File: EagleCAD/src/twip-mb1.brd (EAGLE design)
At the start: 81 x 88.9 mm, 11 parts, among them U1 GY-521MPU6050

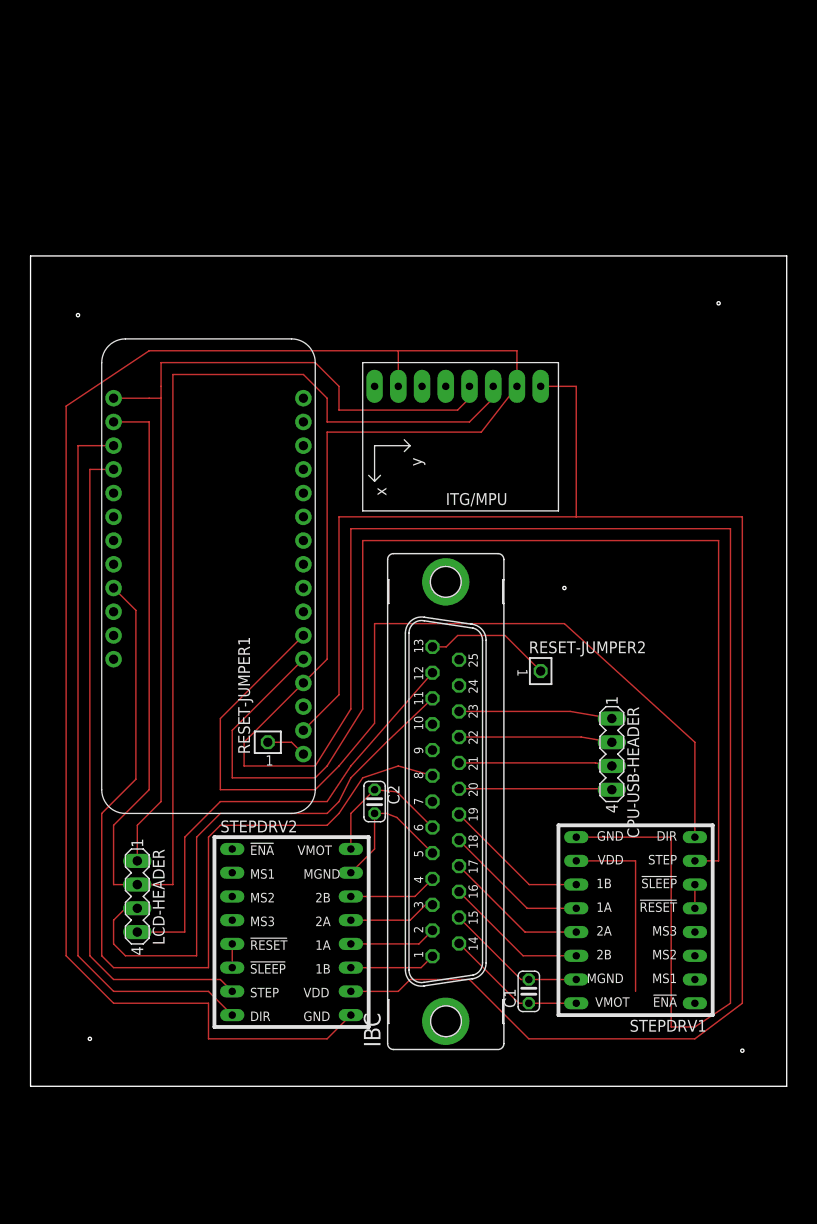
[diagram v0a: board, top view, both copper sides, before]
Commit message: fix LCD header, as decoupling caps
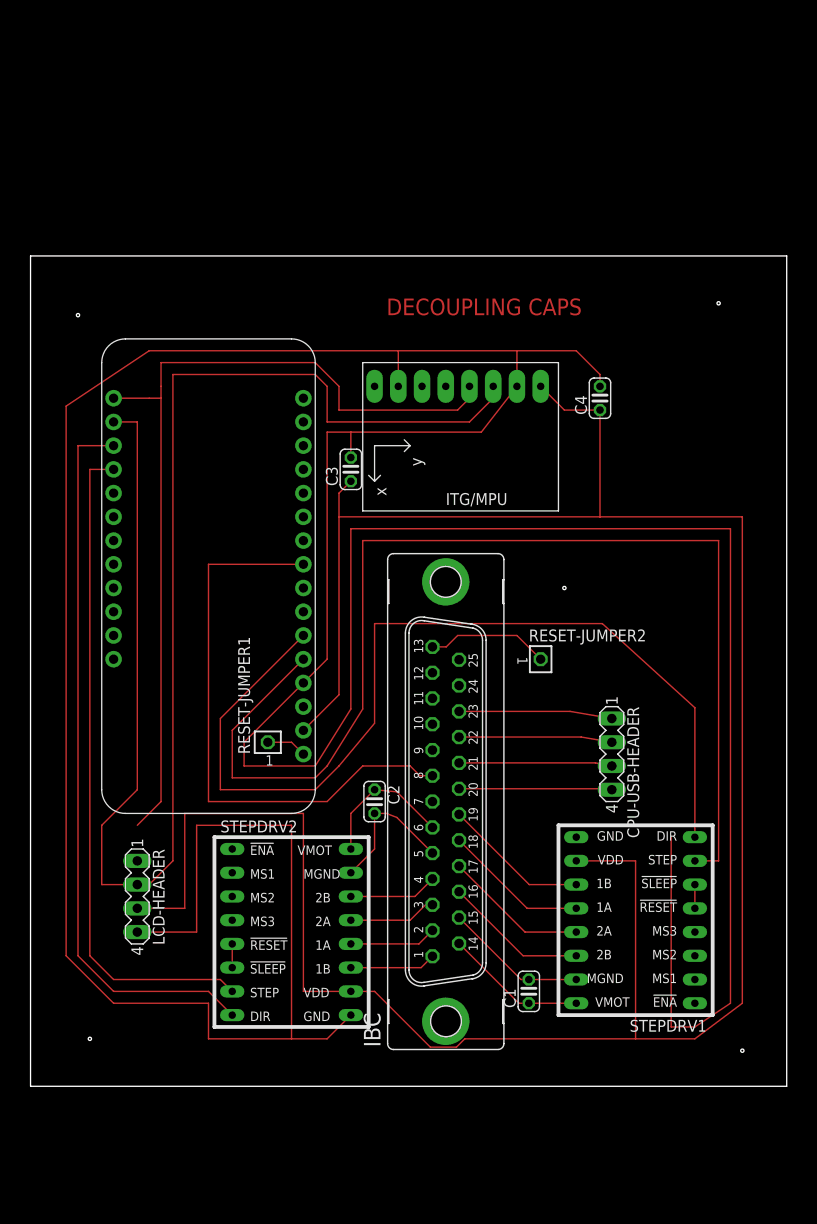
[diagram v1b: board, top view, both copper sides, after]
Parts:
- added C3, C4: 100 uF, rcl:C025-024X044
- moved RESET-JUMPER2 1.27 mm to (61.0, 45.7)
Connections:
- removed net N$11 (its old number): IBC.8, MS2.25
- removed net N$33: IBC.11, LCD-HEADER.3
- removed net N$34: IBC.12, LCD-HEADER.4
- new net N$28: IBC.8, MS2.9
- net 3V: now also C3.1, C4.1, LCD-HEADER.3
- net N$35: now also C3.2, C4.2, LCD-HEADER.4
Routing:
- net N$11 (its old number): track 95.6 -> 0.00 mm
- net 3V: track 204.1 -> 266.3 mm
- net N$28: track 0.00 -> 61.5 mm
- net N$33: track 59.6 -> 0.00 mm
- net N$35: track 379.3 -> 433.8 mm
- net N$34: track 49.9 -> 0.00 mm
- net N$19: track 97.9 -> 94.1 mm
- net N$15: track 99.9 -> 102.2 mm
- net N$11: track 156.1 -> 155.3 mm
- net N$1: track 13.7 -> 13.1 mm
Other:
- board text added: "DECOUPLING CAPS"

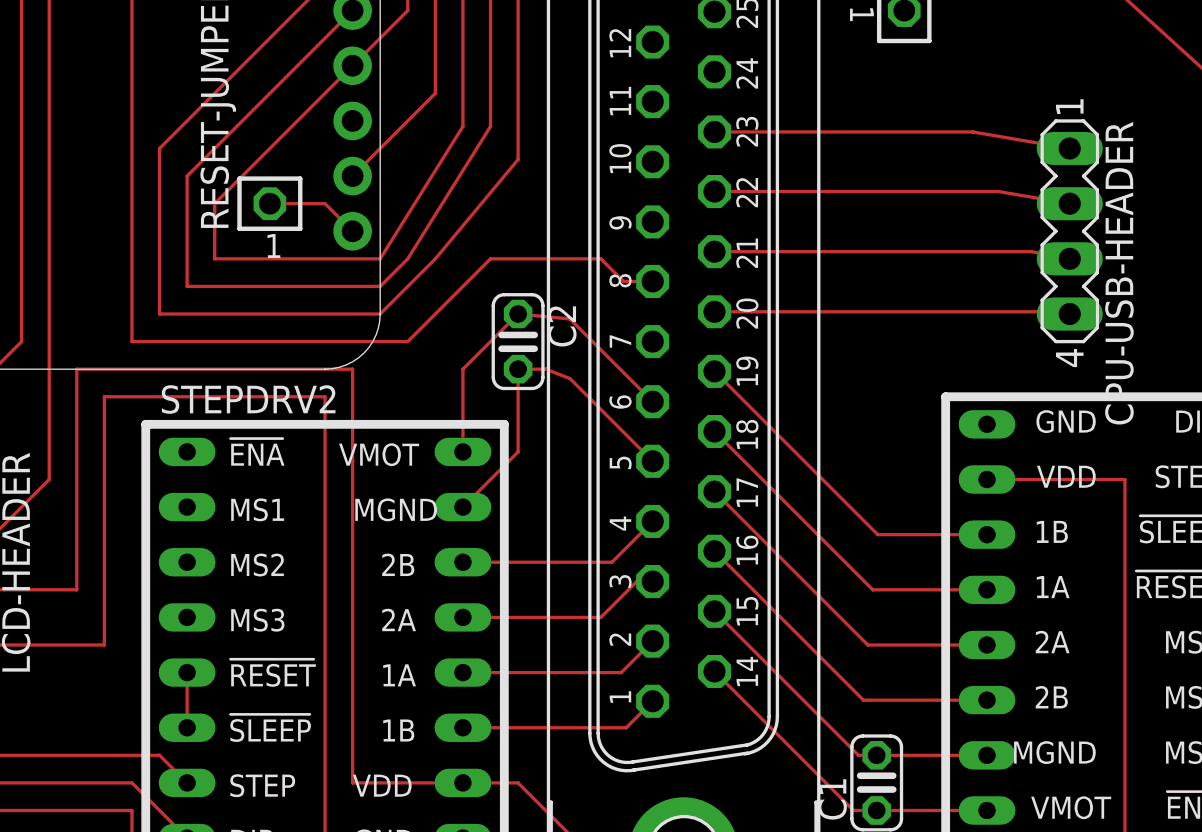
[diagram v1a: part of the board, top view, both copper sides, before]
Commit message: Sep 24 checkpoint has mutually consistent versions of MB and PB layouts, and pinouts documentation
completed layout of peripheral board, with a few retrofits to MB for IBC connector changes. Added a 4 position DIP switch to PB as a way to have jumpers that cross other traces, as I couldn't quite do a single sided layout. All switches go to the right when active, and the voltage regulators, whose 4 legs are represented by two 5 pin headers, are correctly scaled. I'd like to space out the top connector for the stepper motor connections, but the board is at the max size allowed, and Eagle CAD won't allow it to be moved upward.
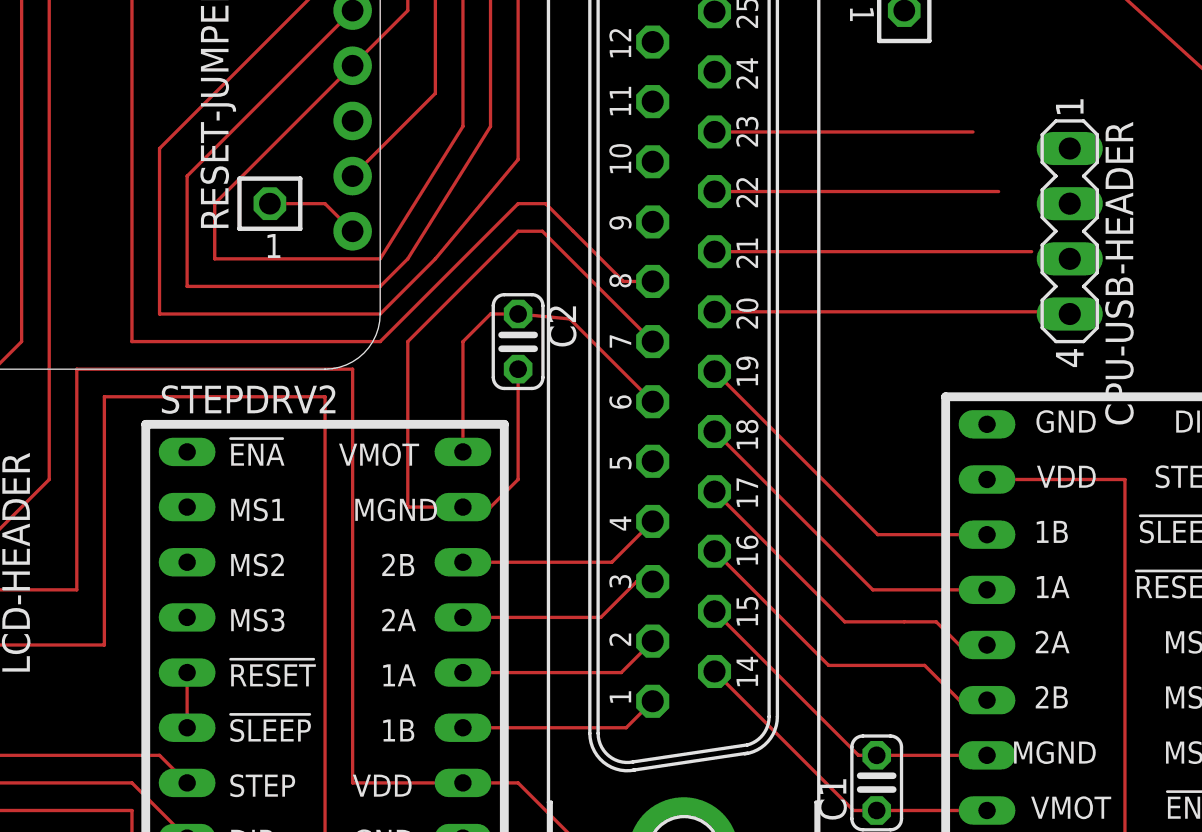
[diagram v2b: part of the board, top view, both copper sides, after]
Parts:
- C1, C2, C3, C4: value 100 uF -> .1 uF
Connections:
- net N$13: now also CPU-USB-HEADER.4; no longer CPU-USB-HEADER.1
- net N$14: now also CPU-USB-HEADER.3; no longer CPU-USB-HEADER.2
- net N$18: now also CPU-USB-HEADER.2; no longer CPU-USB-HEADER.3
- net N$2: now also IBC.7; no longer IBC.5
- net N$30: now also CPU-USB-HEADER.1; no longer CPU-USB-HEADER.4
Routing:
- net N$2: track 15.3 -> 33.8 mm
- net N$13: track 16.4 -> 11.9 mm
- net N$14: track 16.4 -> 13.1 mm
- net N$28: track 61.5 -> 63.7 mm
- net N$18: track 16.4 -> 14.6 mm
- net N$21: track 15.2 -> 15.9 mm
- net N$30: track 16.4 -> 15.8 mm
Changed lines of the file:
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@@
 <attribute name="OC_NEWARK" value="unknown" x="50.8" y="30.48" size="1.778" layer="27" rot="R90" display="off"/>
 </element>
-<element name="C1" library="rcl" library_urn="urn:adsk.eagle:library:334" package="C025-024X044" package3d_urn="urn:adsk.eagle:package:23630/1" value="100 uF" x="59.69" y="10.16" rot="R90">
+<element name="C1" library="rcl" library_urn="urn:adsk.eagle:library:334" package="C025-024X044" package3d_urn="urn:adsk.eagle:package:23630/1" value=".1 uF" x="59.69" y="10.16" rot="R90">
 <attribute name="SPICEPREFIX" value="C" x="59.69" y="10.16" size="1.778" layer="27" rot="R90" display="off"/>
 </element>
-<element name="C2" library="rcl" library_urn="urn:adsk.eagle:library:334" package="C025-024X044" package3d_urn="urn:adsk.eagle:package:23630/1" value="100 uF" x="43.18" y="30.48" rot="R270">
+<element name="C2" library="rcl" library_urn="urn:adsk.eagle:library:334" package="C025-024X044" package3d_urn="urn:adsk.eagle:package:23630/1" value=".1 uF" x="43.18" y="30.48" rot="R270">
 <attribute name="SPICEPREFIX" value="C" x="43.18" y="30.48" size="1.778" layer="27" rot="R270" display="off"/>
 </element>
@@
 <element name="U1" library="gy-521" package="GY-521" value="GY-521MPU6050" x="52.07" y="66.04" rot="R270"/>
 <element name="MS2" library="microbuilder" package="FEATHERWING_NOHOLES" value="FEATHERWING_NOHOLES" x="36.83" y="29.21" rot="R90"/>
-<element name="C3" library="rcl" library_urn="urn:adsk.eagle:library:334" package="C025-024X044" package3d_urn="urn:adsk.eagle:package:23630/1" value="100 uF" x="40.64" y="66.04" rot="R90">
+<element name="C3" library="rcl" library_urn="urn:adsk.eagle:library:334" package="C025-024X044" package3d_urn="urn:adsk.eagle:package:23630/1" value=".1 uF" x="40.64" y="66.04" rot="R90">
 <attribute name="SPICEPREFIX" value="C" x="40.64" y="66.04" size="1.778" layer="27" rot="R90" display="off"/>
 </element>
-<element name="C4" library="rcl" library_urn="urn:adsk.eagle:library:334" package="C025-024X044" package3d_urn="urn:adsk.eagle:package:23630/1" value="100 uF" x="67.31" y="73.66" rot="R90">
+<element name="C4" library="rcl" library_urn="urn:adsk.eagle:library:334" package="C025-024X044" package3d_urn="urn:adsk.eagle:package:23630/1" value=".1 uF" x="67.31" y="73.66" rot="R90">
 <attribute name="SPICEPREFIX" value="C" x="67.31" y="73.66" size="1.778" layer="27" rot="R90" display="off"/>
 </element>
@@
 <wire x1="15.24" y1="11.43" x2="12.7" y2="13.97" width="0.1524" layer="1"/>
 </signal>
-<signal name="N$17">
-<contactref element="STEPDRV2" pad="16"/>
-<contactref element="C2" pad="1"/>
-<contactref element="IBC" pad="6"/>
-<wire x1="43.18" y1="31.75" x2="40.64" y2="29.21" width="0.1524" layer="1"/>
-<wire x1="45.5676" y1="31.5214" x2="49.3776" y2="27.7114" width="0.1524" layer="1"/>
-<wire x1="40.64" y1="29.21" x2="40.64" y2="25.4" width="0.1524" layer="1"/>
-<wire x1="43.18" y1="31.75" x2="45.5676" y2="31.5214" width="0.1524" layer="1"/>
-</signal>
 <signal name="N$16">
 <contactref element="RESET-JUMPER1" pad="1"/>
@@
 <contactref element="C2" pad="2"/>
 <contactref element="STEPDRV2" pad="15"/>
-<contactref element="IBC" pad="5"/>
-<wire x1="43.18" y1="25.4" x2="40.64" y2="22.86" width="0.1524" layer="1"/>
-<wire x1="45.5676" y1="28.7782" x2="49.3776" y2="24.9682" width="0.1524" layer="1"/>
-<wire x1="43.18" y1="29.21" x2="44.45" y2="29.21" width="0.1524" layer="1"/>
-<wire x1="44.45" y1="29.21" x2="45.5676" y2="28.7782" width="0.1524" layer="1"/>
-<wire x1="43.18" y1="29.21" x2="43.18" y2="25.4" width="0.1524" layer="1"/>
+<wire x1="43.18" y1="24.13" x2="41.91" y2="22.86" width="0.1524" layer="1"/>
+<wire x1="43.18" y1="29.21" x2="43.18" y2="24.13" width="0.1524" layer="1"/>
+<contactref element="IBC" pad="7"/>
+<wire x1="40.64" y1="22.86" x2="38.1" y2="22.86" width="0.1524" layer="1"/>
+<wire x1="38.1" y1="22.86" x2="38.1" y2="30.48" width="0.1524" layer="1"/>
+<wire x1="38.1" y1="30.48" x2="43.18" y2="35.56" width="0.1524" layer="1"/>
+<wire x1="44.2976" y1="35.56" x2="49.3776" y2="30.48" width="0.1524" layer="1"/>
+<wire x1="43.18" y1="35.56" x2="44.2976" y2="35.56" width="0.1524" layer="1"/>
+<wire x1="41.91" y1="22.86" x2="40.64" y2="22.86" width="0.1524" layer="1"/>
 </signal>
 <signal name="N$3">
 <contactref element="STEPDRV1" pad="14"/>
 <contactref element="IBC" pad="16"/>
-<wire x1="52.2224" y1="20.828" x2="59.0804" y2="13.97" width="0.1524" layer="1"/>
-<wire x1="59.0804" y1="13.97" x2="64.77" y2="13.97" width="0.1524" layer="1"/>
+<wire x1="52.2224" y1="20.828" x2="57.4802" y2="15.5702" width="0.1524" layer="1"/>
+<wire x1="63.5" y1="13.97" x2="64.77" y2="13.97" width="0.1524" layer="1"/>
+<wire x1="61.8998" y1="15.5702" x2="63.5" y2="13.97" width="0.1524" layer="1"/>
+<wire x1="57.4802" y1="15.5702" x2="61.8998" y2="15.5702" width="0.1524" layer="1"/>
 </signal>
 <signal name="N$4">
 <contactref element="STEPDRV1" pad="13"/>
 <contactref element="IBC" pad="17"/>
-<wire x1="52.2224" y1="23.5712" x2="59.2836" y2="16.51" width="0.1524" layer="1"/>
-<wire x1="59.2836" y1="16.51" x2="64.77" y2="16.51" width="0.1524" layer="1"/>
+<wire x1="52.2224" y1="23.5712" x2="58.2168" y2="17.5768" width="0.1524" layer="1"/>
+<wire x1="58.2168" y1="17.5768" x2="60.96" y2="17.5768" width="0.1524" layer="1"/>
+<wire x1="60.96" y1="17.5768" x2="62.4332" y2="17.5768" width="0.1524" layer="1"/>
+<wire x1="62.4332" y1="17.5768" x2="63.5" y2="16.51" width="0.1524" layer="1"/>
+<wire x1="63.5" y1="16.51" x2="64.77" y2="16.51" width="0.1524" layer="1"/>
 </signal>
 <signal name="N$6">
@@
 <signal name="N$13">
 <contactref element="IBC" pad="23"/>
-<contactref element="CPU-USB-HEADER" pad="1"/>
-<wire x1="64.124540625" y1="40.132" x2="68.58" y2="39.37" width="0.1524" layer="1"/>
 <wire x1="52.2224" y1="40.132" x2="64.124540625" y2="40.132" width="0.1524" layer="1"/>
+<contactref element="CPU-USB-HEADER" pad="4"/>
+<wire x1="64.124540625" y1="40.132" x2="68.58" y2="31.75" width="0" layer="19" extent="1-1"/>
 </signal>
 <signal name="N$14">
 <contactref element="IBC" pad="22"/>
-<contactref element="CPU-USB-HEADER" pad="2"/>
-<wire x1="65.30254375" y1="37.3888" x2="68.58" y2="36.83" width="0.1524" layer="1"/>
 <wire x1="52.2224" y1="37.3888" x2="65.30254375" y2="37.3888" width="0.1524" layer="1"/>
+<contactref element="CPU-USB-HEADER" pad="3"/>
+<wire x1="65.30254375" y1="37.3888" x2="68.58" y2="34.29" width="0" layer="19" extent="1-1"/>
 </signal>
 <signal name="N$18">
 <contactref element="IBC" pad="21"/>
-<contactref element="CPU-USB-HEADER" pad="3"/>
-<wire x1="66.82481875" y1="34.6202" x2="68.58" y2="34.29" width="0.1524" layer="1"/>
 <wire x1="52.2224" y1="34.6202" x2="66.82481875" y2="34.6202" width="0.1524" layer="1"/>
+<contactref element="CPU-USB-HEADER" pad="2"/>
+<wire x1="66.82481875" y1="34.6202" x2="68.58" y2="36.83" width="0" layer="19" extent="1-1"/>
 </signal>
 <signal name="N$30">
 <contactref element="IBC" pad="20"/>
-<contactref element="CPU-USB-HEADER" pad="4"/>
-<wire x1="68.06474375" y1="31.8516" x2="68.58" y2="31.75" width="0.1524" layer="1"/>
 <wire x1="52.2224" y1="31.8516" x2="68.06474375" y2="31.8516" width="0.1524" layer="1"/>
+<contactref element="CPU-USB-HEADER" pad="1"/>
+<wire x1="68.06474375" y1="31.8516" x2="68.58" y2="39.37" width="0" layer="19" extent="1-1"/>
 </signal>
 <signal name="N$35">
@@
 <contactref element="IBC" pad="8"/>
 <wire x1="49.3776" y1="33.2486" x2="48.0314" y2="33.2486" width="0.1524" layer="1"/>
-<wire x1="48.0314" y1="33.2486" x2="46.99" y2="34.29" width="0.1524" layer="1"/>
-<wire x1="46.99" y1="34.29" x2="41.91" y2="34.29" width="0.1524" layer="1"/>
-<wire x1="41.91" y1="34.29" x2="38.1" y2="30.48" width="0.1524" layer="1"/>
-<wire x1="38.1" y1="30.48" x2="25.4" y2="30.48" width="0.1524" layer="1"/>
+<wire x1="48.0314" y1="33.2486" x2="45.72" y2="35.56" width="0.1524" layer="1"/>
+<wire x1="36.83" y1="30.48" x2="25.4" y2="30.48" width="0.1524" layer="1"/>
 <wire x1="25.4" y1="30.48" x2="25.4" y2="55.88" width="0.1524" layer="1"/>
 <wire x1="25.4" y1="55.88" x2="35.56" y2="55.88" width="0.1524" layer="1"/>
+<wire x1="36.83" y1="30.48" x2="43.18" y2="36.83" width="0.1524" layer="1"/>
+<wire x1="43.18" y1="36.83" x2="44.45" y2="36.83" width="0.1524" layer="1"/>
+<wire x1="44.45" y1="36.83" x2="45.72" y2="35.56" width="0.1524" layer="1"/>
 </signal>
 <signal name="N$11">
@@
 <wire x1="17.78" y1="71.12" x2="17.78" y2="31.75" width="0.1524" layer="1"/>
 </signal>
+<signal name="N$21">
+<contactref element="IBC" pad="6"/>
+<contactref element="STEPDRV2" pad="16"/>
+<contactref element="C2" pad="1"/>
+<wire x1="41.91" y1="31.75" x2="40.64" y2="30.48" width="0.1524" layer="1"/>
+<wire x1="40.64" y1="30.48" x2="40.64" y2="25.4" width="0.1524" layer="1"/>
+<wire x1="45.5676" y1="31.5214" x2="43.18" y2="31.75" width="0.1524" layer="1"/>
+<wire x1="43.18" y1="31.75" x2="41.91" y2="31.75" width="0.1524" layer="1"/>
+<wire x1="49.3776" y1="27.7114" x2="45.5676" y2="31.5214" width="0.1524" layer="1"/>
+</signal>
 </signals>
